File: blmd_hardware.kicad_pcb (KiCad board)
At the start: 4 copper layers, 50 x 28.5 mm, 71 parts, among them J1 MR30PW-F, J2 control, J3 GND, J4 12V, J5 STLink-V3, J6 GH4, Q1 RH6G040CH, Q2 RH6G040CH, Q3 RH6G040CH, Q4 RH6G040CH, Q5 RH6G040CH, Q6 RH6G040CH, SW1 reset, SW2 SW_DIP_x02, U1 STSPIN32G4, U2 ISO6520, U3 TCAN3414DDFR, U4 ACS711KEXLT-31AB, U5 ACS711KEXLT-31AB

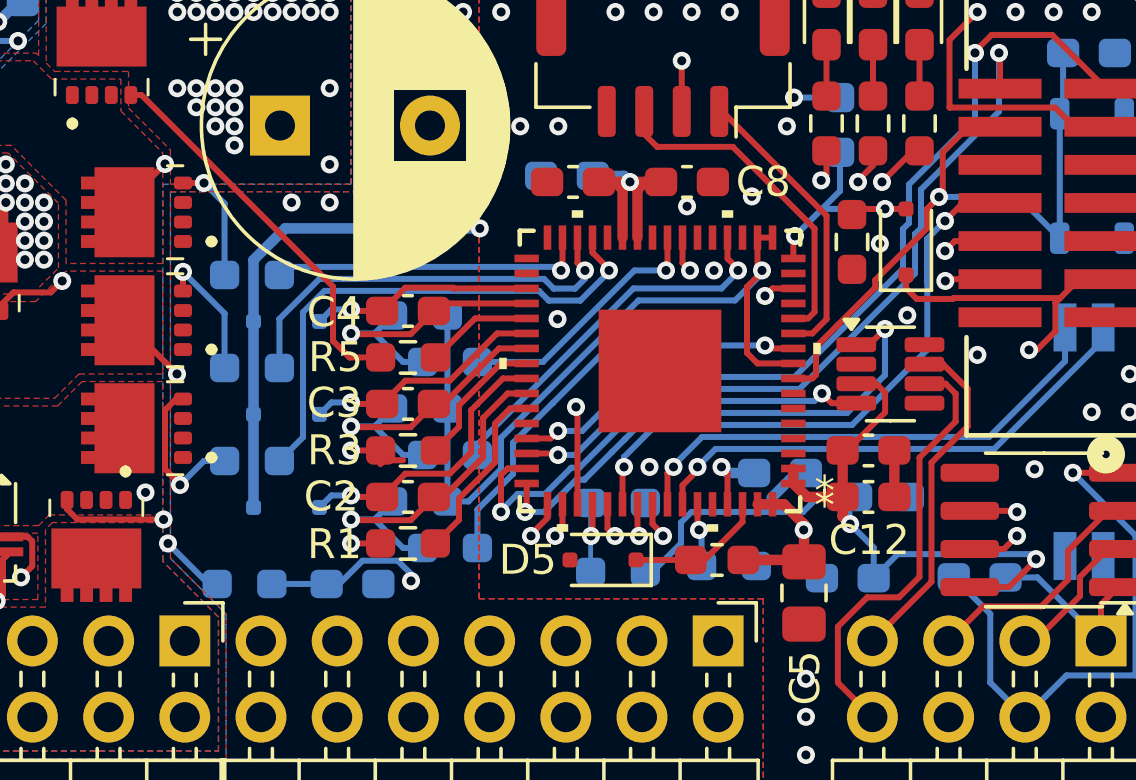
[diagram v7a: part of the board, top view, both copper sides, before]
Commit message: change : diode from sod-323f to sod-323
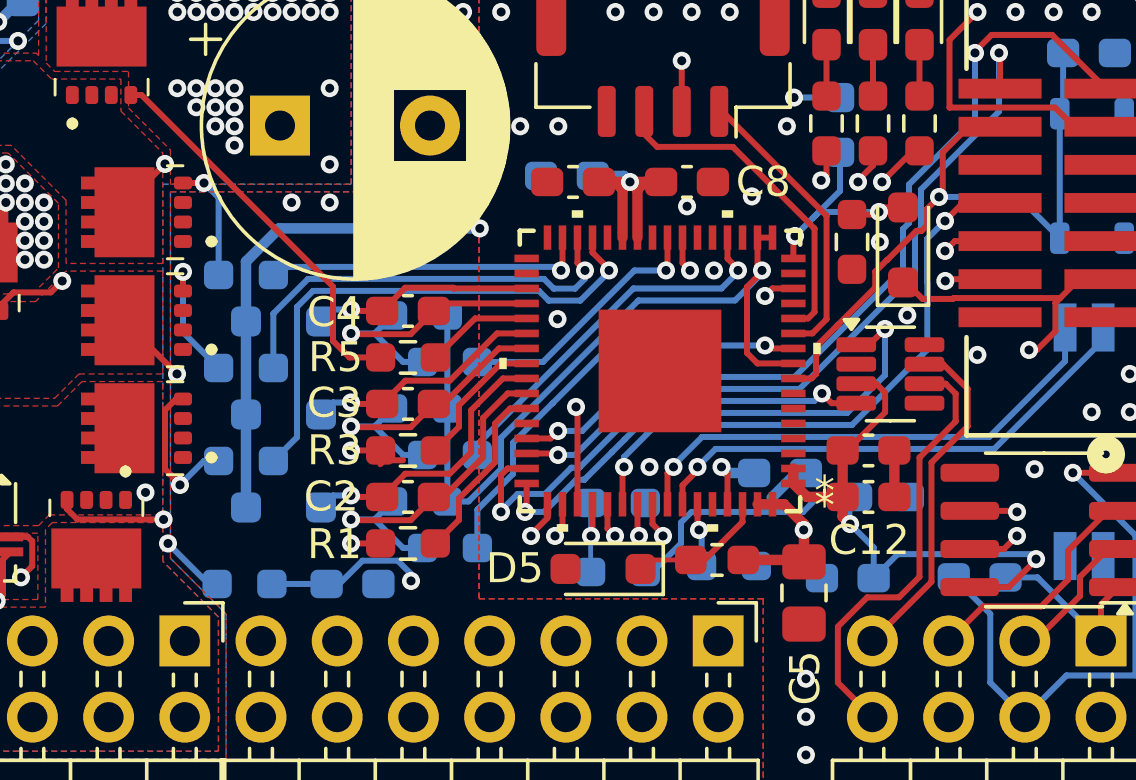
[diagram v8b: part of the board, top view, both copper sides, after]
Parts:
- D1, D2, D3, D4: value schot -> 1N5819WS; footprint Diode_SMD:D_SOD-323F -> Diode_SMD:D_SOD-323_HandSoldering
- D5: value fast rec -> 1N4148WS; footprint Diode_SMD:D_SOD-323F -> Diode_SMD:D_SOD-323_HandSoldering
- moved D5 0.30 mm to (81.5, 70.0)
- moved R2 0.20 mm to (69.6, 66.4)
- moved R4 0.20 mm to (69.6, 63.3)
- moved R6 0.20 mm to (69.6, 60.2)
- moved D1 0.14 mm to (91.5, 59.2)
- moved D2 0.10 mm to (70.8, 68.0)
- moved D3 0.10 mm to (70.8, 64.8)
- moved D4 0.10 mm to (70.8, 61.8)
